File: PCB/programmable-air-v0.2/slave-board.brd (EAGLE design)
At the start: 97.7 x 49 mm, 37 parts, among them IC1 INA126U, IC3 LM358MX, Q1 600mA/40V, Q2 600mA/40V, Q3 600mA/40V

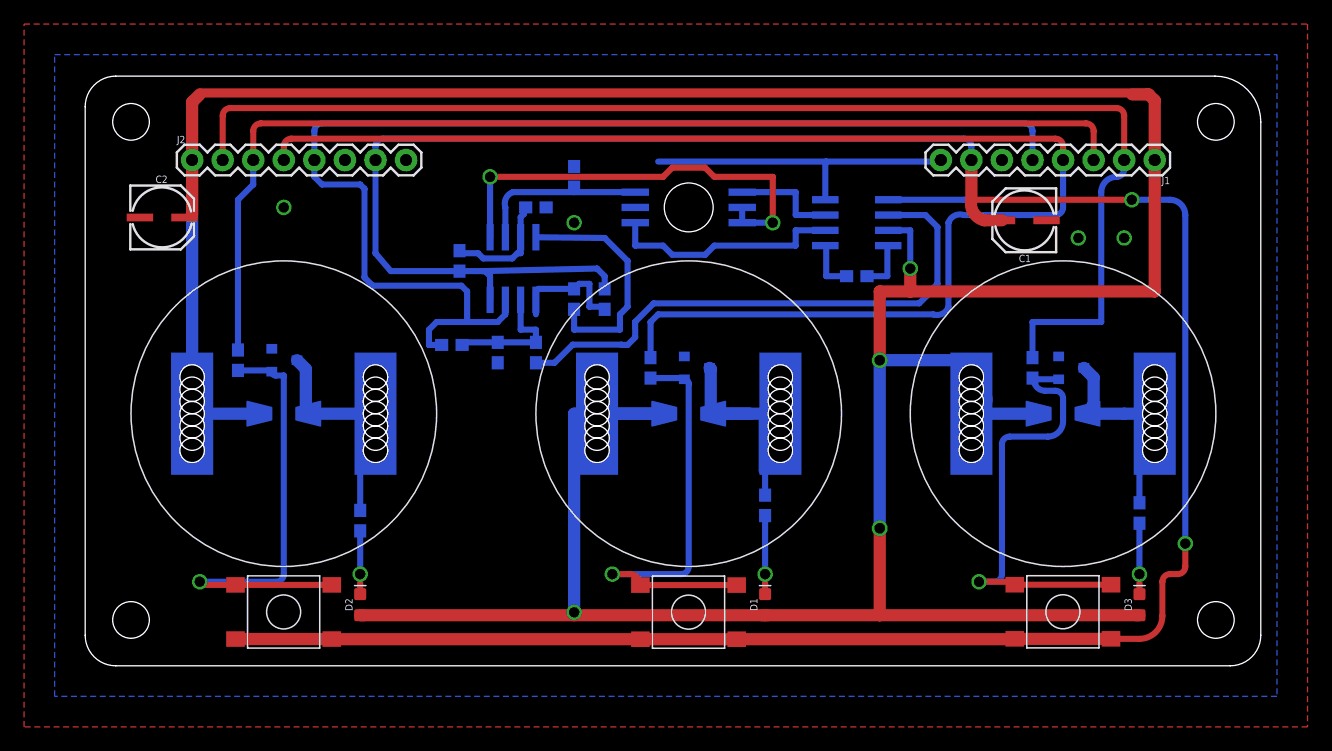
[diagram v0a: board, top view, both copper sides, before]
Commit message: Master board + Slave board in single PCB ready.
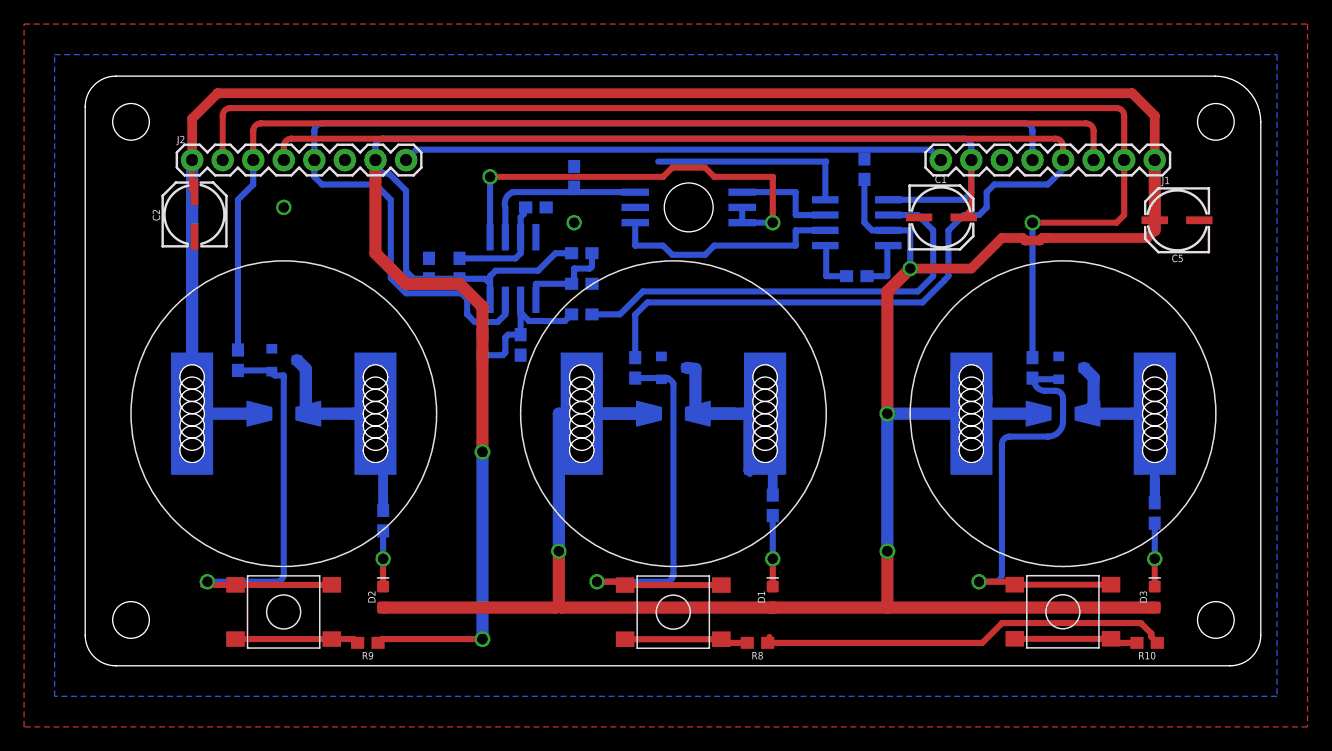
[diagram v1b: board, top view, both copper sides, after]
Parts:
- added C3, C4: 1.0uF, SparkFun-Capacitors:0603
- added C5: 22uF, SparkFun-Capacitors:PANASONIC_C
- added R10, R8, R9: 1k, SparkFun-Resistors:0603
- moved C1 7.01 mm to (71.1, 37.5), turned to 0 degrees
- moved R22 4.96 mm to (41.3, 29.2), turned to 0 degrees
- moved R18 4.26 mm to (41.3, 34.3), turned to 0 degrees
- moved R19 2.54 mm to (33.0, 26.7), turned to 270 degrees
- moved C2 2.54 mm to (8.89, 37.5), turned to 90 degrees
- moved R23 2.01 mm to (36.2, 26.7)
- moved D2 2.01 mm to (24.8, 5.71)
- moved R6 1.91 mm to (24.8, 12.1)
- moved Q1 1.90 mm to (48.9, 24.8)
- moved D3 1.42 mm to (88.9, 5.71)
- moved R12 1.42 mm to (41.3, 31.8), turned to 0 degrees
- moved R7 1.27 mm to (88.9, 12.7)
- moved R1 1.27 mm to (45.7, 24.8)
- moved U$2 1.27 mm to (48.9, 21.0)
- moved U$5 1.27 mm to (48.9, 21.0)
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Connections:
- removed net N$15: C1.+, IC1.5, IC3.8, J1.7, J2.7, R18.2, R21.1, U$10.P$1, U$10.P$3, U$8.P$1, U$8.P$3, U$9.P$1, U$9.P$3
- removed net VIN: C2.+, D1.A, D2.A, D3.A, IC1.7, J1.1, J2.1, U$2.P$1, U$3.P$1, U$4.P$1, U$5.P$1, U$6.P$1, U$7.P$1
- new net N$17: C2.+, C4.1, C5.+, D1.A, D2.A, D3.A, IC1.7, J1.1, J2.1, U$2.P$1, U$3.P$1, U$4.P$1, U$5.P$1, U$6.P$1, U$7.P$1
- new net N$21: R8.2, U$8.P$1, U$8.P$3
- new net N$22: R9.2, U$9.P$1, U$9.P$3
- new net N$23: R10.2, U$10.P$1, U$10.P$3
- new net N$28: C1.+, C3.1, IC1.5, IC3.8, J1.7, J2.7, R10.1, R18.2, R21.1, R8.1, R9.1
- net GND: now also C3.2, C4.2, C5.-
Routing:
- net VIN: track 397.2 -> 0.00 mm, vias 4 -> 0
- net N$17: track 0.00 -> 324.4 mm, vias 0 -> 4
- net N$15: track 275.3 -> 0.00 mm, vias 2 -> 0
- net N$28: track 0.00 -> 185.9 mm, vias 0 -> 2
- net GND: track 46.8 -> 62.7 mm, vias 4 -> 2
- net N$23: track 0.00 -> 10.3 mm
- net N$22: track 0.00 -> 10.3 mm
- net N$21: track 0.00 -> 10.3 mm
- net N$9: track 22.4 -> 31.5 mm
- net N$16: track 46.1 -> 37.7 mm
- net N$13: track 100.4 -> 94.4 mm
- net N$8: track 20.2 -> 25.9 mm
- net N$7: track 23.4 -> 25.4 mm
- net N$30: track 9.88 -> 8.28 mm
- net N$5: track 105.7 -> 107.3 mm, vias 0 -> 1
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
